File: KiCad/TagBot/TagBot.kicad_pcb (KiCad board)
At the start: 4 copper layers, 54 x 57 mm, 76 parts, among them IC101 ADXL343BCCZ-RL, J101 Conn_ST_STDC14, J102 Conn_01x06, J103 Conn_01x03, J104 Conn_01x06, J105 Conn_01x02, J106 Conn_01x08, J107 Conn_01x06, J111 Conn_01x04, SW101 SW_Push, SW102 SW_Push, U101 STM32G431CBUx, U201 ZXBM5210-SP, U301 ZXBM5210-SP, U401 MP1475S, U501 BU33SD5WG-TR, Y101 Crystal

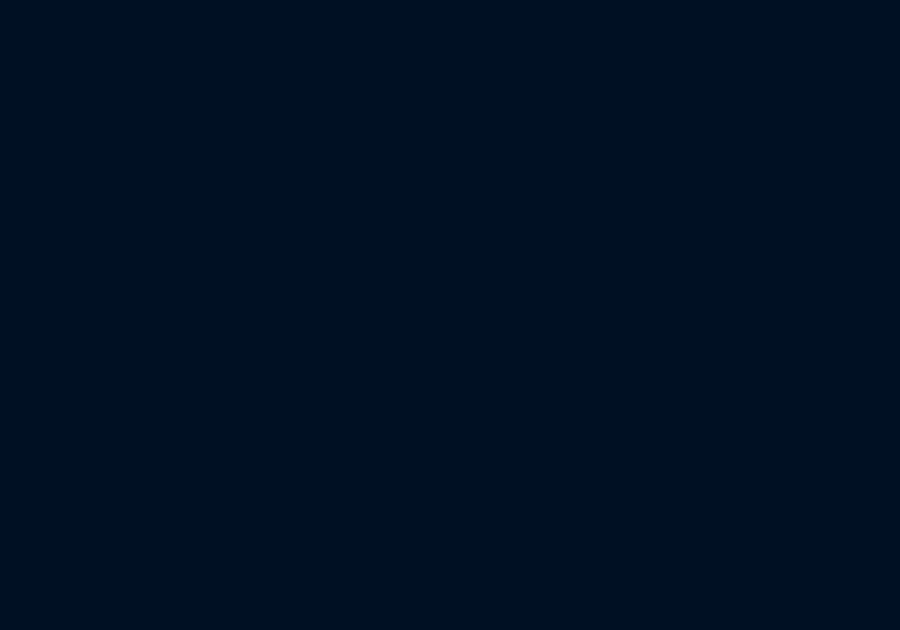
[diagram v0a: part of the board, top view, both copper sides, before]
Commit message: ajout résistance capteurs
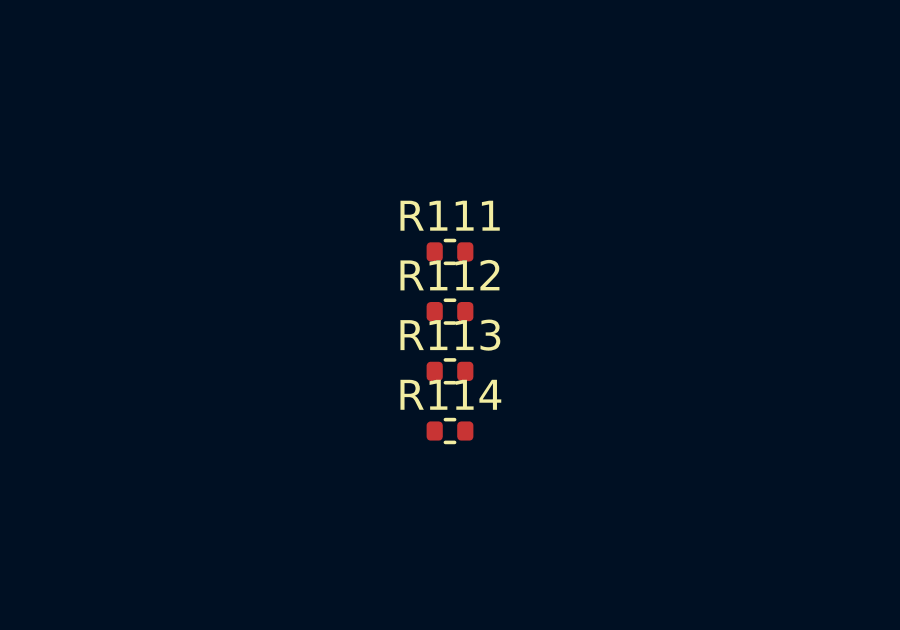
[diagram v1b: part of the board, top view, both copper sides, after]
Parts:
- added R111: 100, Resistor_SMD:R_0402_1005Metric, F.Cu at (150.0, 42.2)
- added R112: 100, Resistor_SMD:R_0402_1005Metric, F.Cu at (150.0, 44.2)
- added R113: 100, Resistor_SMD:R_0402_1005Metric, F.Cu at (150.0, 46.2)
- added R114: 100, Resistor_SMD:R_0402_1005Metric, F.Cu at (150.0, 48.1)
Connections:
- J107 pad 1: /Capteur_dist_S -> Net-(J107-Pin_1)
- J107 pad 2: /Capteur_dist_N -> Net-(J107-Pin_2)
- J107 pad 3: /Capteur_dist_W -> Net-(J107-Pin_3)
- J107 pad 4: /Capteur_dist_E -> Net-(J107-Pin_4)

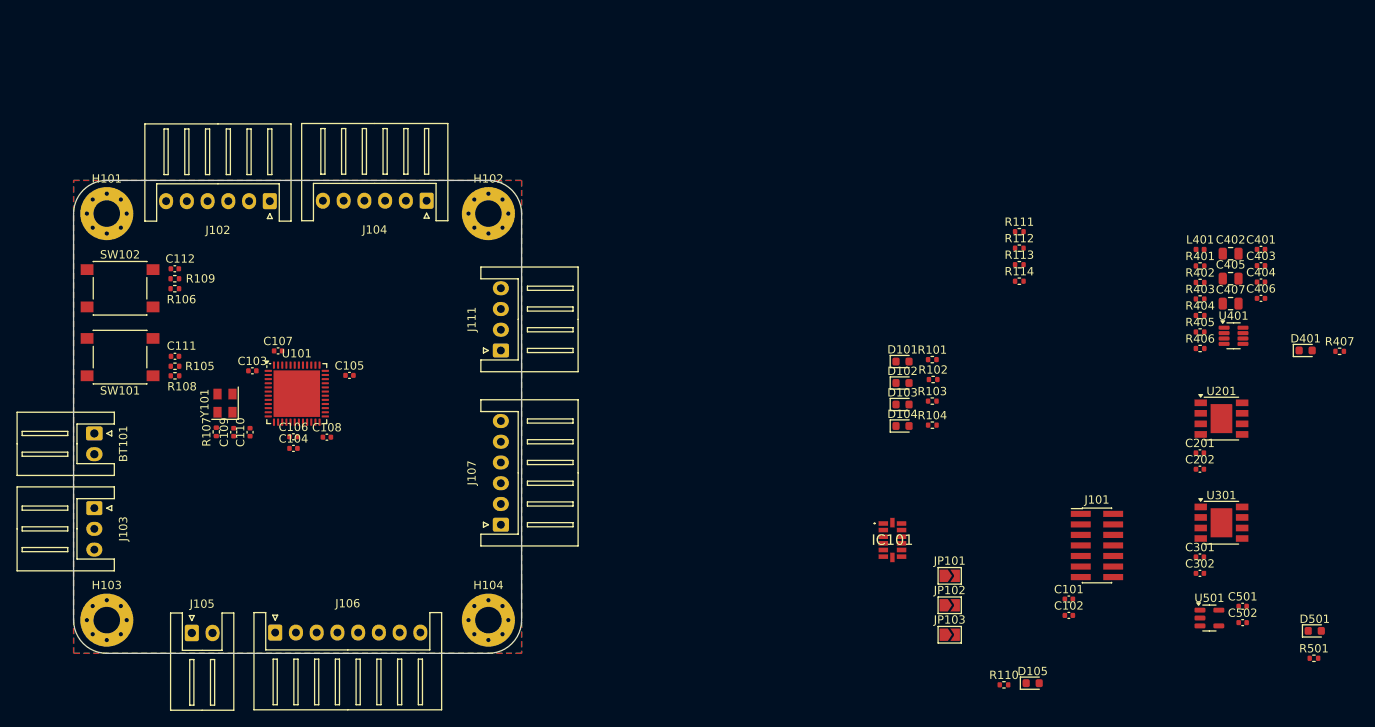
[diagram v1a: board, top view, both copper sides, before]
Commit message: correction schema kicad
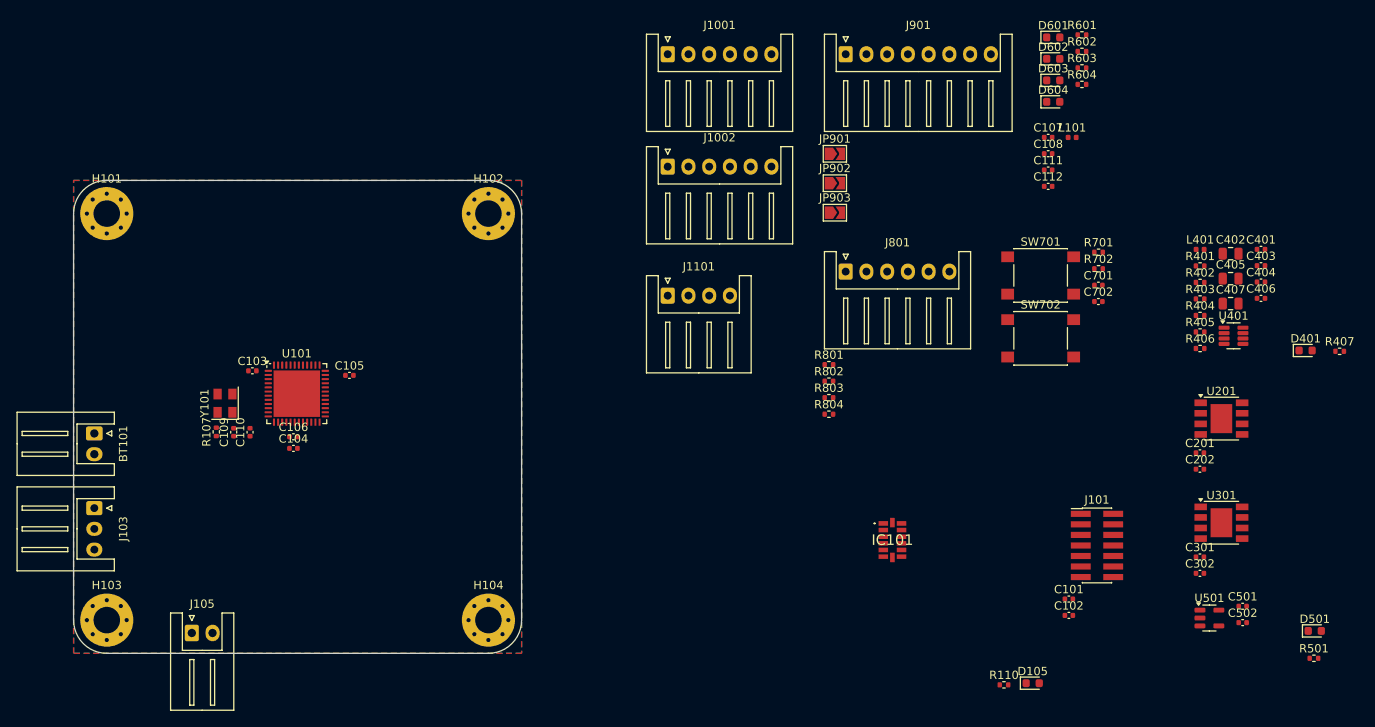
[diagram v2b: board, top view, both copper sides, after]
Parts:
- removed D101, D102, D103, D104: LED, LED_SMD:LED_0603_1608Metric
- removed J102, J104, J107: Conn_01x06, Connector_JST:JST_XH_S6B-XH-A_1x06_P2.50mm_Horizontal
- removed J106: Conn_01x08, Connector_JST:JST_XH_S8B-XH-A_1x08_P2.50mm_Horizontal
- removed J111: Conn_01x04, Connector_JST:JST_XH_S4B-XH-A_1x04_P2.50mm_Horizontal
- removed JP101, JP102, JP103: SolderJumper_2_Open, Jumper:SolderJumper-2_P1.3mm_Open_TrianglePad1.0x1.5mm
- removed R101: 1.3k, Resistor_SMD:R_0402_1005Metric
- removed R102, R103, R104, R111, R112, R113, R114: 100, Resistor_SMD:R_0402_1005Metric
- removed R105, R106: 100k, Resistor_SMD:R_0402_1005Metric
- removed R108, R109: 1k, Resistor_SMD:R_0402_1005Metric
- removed SW101, SW102: SW_Push, Button_Switch_SMD:SW_Push_1P1T_NO_6x6mm_H9.5mm
- added C701: 10n, Capacitor_SMD:C_0402_1005Metric, F.Cu at (159.5, 48.6)
- added C702: 100n, Capacitor_SMD:C_0402_1005Metric, F.Cu at (159.5, 50.6)
- added D601: LED, LED_SMD:LED_0603_1608Metric, F.Cu at (154.1, 18.8)
- added D602: LED, LED_SMD:LED_0603_1608Metric, F.Cu at (154.1, 21.4)
- added D603: LED, LED_SMD:LED_0603_1608Metric, F.Cu at (154.1, 23.9)
- added D604: LED, LED_SMD:LED_0603_1608Metric, F.Cu at (154.1, 26.5)
- added J1001: Conn_01x06, Connector_JST:JST_XH_S6B-XH-A_1x06_P2.50mm_Horizontal, F.Cu at (107.6, 20.8)
- added J1002: Conn_01x06, Connector_JST:JST_XH_S6B-XH-A_1x06_P2.50mm_Horizontal, F.Cu at (107.6, 34.3)
- added J1101: Conn_01x04, Connector_JST:JST_XH_S4B-XH-A_1x04_P2.50mm_Horizontal, F.Cu at (107.6, 49.9)
- added J801: Conn_01x06, Connector_JST:JST_XH_S6B-XH-A_1x06_P2.50mm_Horizontal, F.Cu at (129.1, 47.0)
- added J901: Conn_01x08, Connector_JST:JST_XH_S8B-XH-A_1x08_P2.50mm_Horizontal, F.Cu at (129.1, 20.8)
- added JP901: SolderJumper_2_Open, Jumper:SolderJumper-2_P1.3mm_Open_TrianglePad1.0x1.5mm, F.Cu at (127.8, 32.8)
- added JP902: SolderJumper_2_Open, Jumper:SolderJumper-2_P1.3mm_Open_TrianglePad1.0x1.5mm, F.Cu at (127.8, 36.3)
- added JP903: SolderJumper_2_Open, Jumper:SolderJumper-2_P1.3mm_Open_TrianglePad1.0x1.5mm, F.Cu at (127.8, 39.9)
- added L101: 47n, Inductor_SMD:L_0402_1005Metric, F.Cu at (156.4, 30.8)
- added R601: 300, Resistor_SMD:R_0402_1005Metric, F.Cu at (157.5, 18.5)
- added R602: 300, Resistor_SMD:R_0402_1005Metric, F.Cu at (157.5, 20.4)
- added R603: 1.3k, Resistor_SMD:R_0402_1005Metric, F.Cu at (157.5, 22.4)
- added R604: 300, Resistor_SMD:R_0402_1005Metric, F.Cu at (157.5, 24.4)
- added R701: 10k, Resistor_SMD:R_0402_1005Metric, F.Cu at (159.5, 44.7)
- added R702: 10k, Resistor_SMD:R_0402_1005Metric, F.Cu at (159.5, 46.6)
- added R801: 100, Resistor_SMD:R_0402_1005Metric, F.Cu at (127.0, 58.2)
- added R802: 100, Resistor_SMD:R_0402_1005Metric, F.Cu at (127.0, 60.2)
- added R803: 100, Resistor_SMD:R_0402_1005Metric, F.Cu at (127.0, 62.2)
- added R804: 100, Resistor_SMD:R_0402_1005Metric, F.Cu at (127.0, 64.2)
- added SW701: SW_Push, Button_Switch_SMD:SW_Push_1P1T_NO_6x6mm_H9.5mm, F.Cu at (152.6, 47.5)
- added SW702: SW_Push, Button_Switch_SMD:SW_Push_1P1T_NO_6x6mm_H9.5mm, F.Cu at (152.6, 55.0)
- C108, C111: value 100n -> 1u
- C112: value 100n -> 10n
- C201, C301: value 500n -> 1u
- C202, C302: value 500n -> 10u
- R501: value 100 -> 300
- moved C111 107.6 mm to (153.5, 34.8), turned to 0 degrees
- moved C112 105.7 mm to (153.5, 36.7), turned to 0 degrees
- moved C107 96.3 mm to (153.5, 30.8)
- moved C108 93.4 mm to (153.5, 32.8)
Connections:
- C107 pad 1: +3.3V -> GND
- C107 pad 2: GND -> +3.3VA
- C108 pad 1: +3.3V -> GND
- C108 pad 2: +3.3V -> +3.3VA
- C111 pad 1: /NRST -> GND
- C111 pad 2: GND -> +3.3VA
- C112 pad 1: /BTN_CAT_MOUSE -> GND
- C112 pad 2: GND -> +3.3VA
- C402 pad 1: /Régulateur 5V/7.2V -> /Valim
- C403 pad 1: /Régulateur 5V/7.2V -> /Valim
- J101 pad 12: /NRST -> +3.3V
- R401 pad 1: /Régulateur 5V/7.2V -> /Valim
- U101 pad 20: +3.3V -> +3.3VA
- U101 pad 21: +3.3V -> +3.3VA
- U101 pad 7: /NRST -> +3.3V
- U401 pad 2: /Régulateur 5V/7.2V -> /Valim

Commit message: placement pcb 2
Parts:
- L101: value 47n -> 39n; footprint Inductor_SMD:L_0402_1005Metric -> Inductor_SMD:L_0603_1608Metric
- L401: footprint Inductor_SMD:L_0402_1005Metric -> Library:Power Inductors - SMD WE-LQS 4.7uH
- moved R407 135.6 mm to (53.4, 66.0), turned to 180 degrees
- moved D401 134.3 mm to (50.6, 66.0)
- moved C406 131.7 mm to (48.9, 70.2), turned to -90 degrees
- moved C401 129.3 mm to (52.1, 68.3)
- moved C405 128.1 mm to (50.0, 73.5), turned to -90 degrees
- moved C407 125.0 mm to (52.5, 73.5), turned to -90 degrees
- moved C402 123.7 mm to (56.0, 76.9)
- moved L401 123.4 mm to (53.1, 78.3), turned to 180 degrees
- moved C404 123.4 mm to (58.5, 74.2), turned to -90 degrees
- moved C403 123.4 mm to (58.5, 72.2), turned to 90 degrees
- moved R405 123.0 mm to (49.6, 68.3)
- moved R406 122.3 mm to (50.2, 70.1), turned to -90 degrees
- moved R404 121.4 mm to (51.8, 70.1), turned to 90 degrees
- moved U401 121.2 mm to (56.0, 73.1), turned to 90 degrees
- moved R402 120.8 mm to (53.0, 70.1), turned to -90 degrees
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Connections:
- C101 pad 1: +3.3V -> GND
- C102 pad 1: +3.3V -> GND
- C702 pad 1: +3.3V -> /NRST
- J101 pad 12: +3.3V -> /NRST
- SW702 pad 1: +3.3V -> /NRST
- U101 pad 7: +3.3V -> /NRST

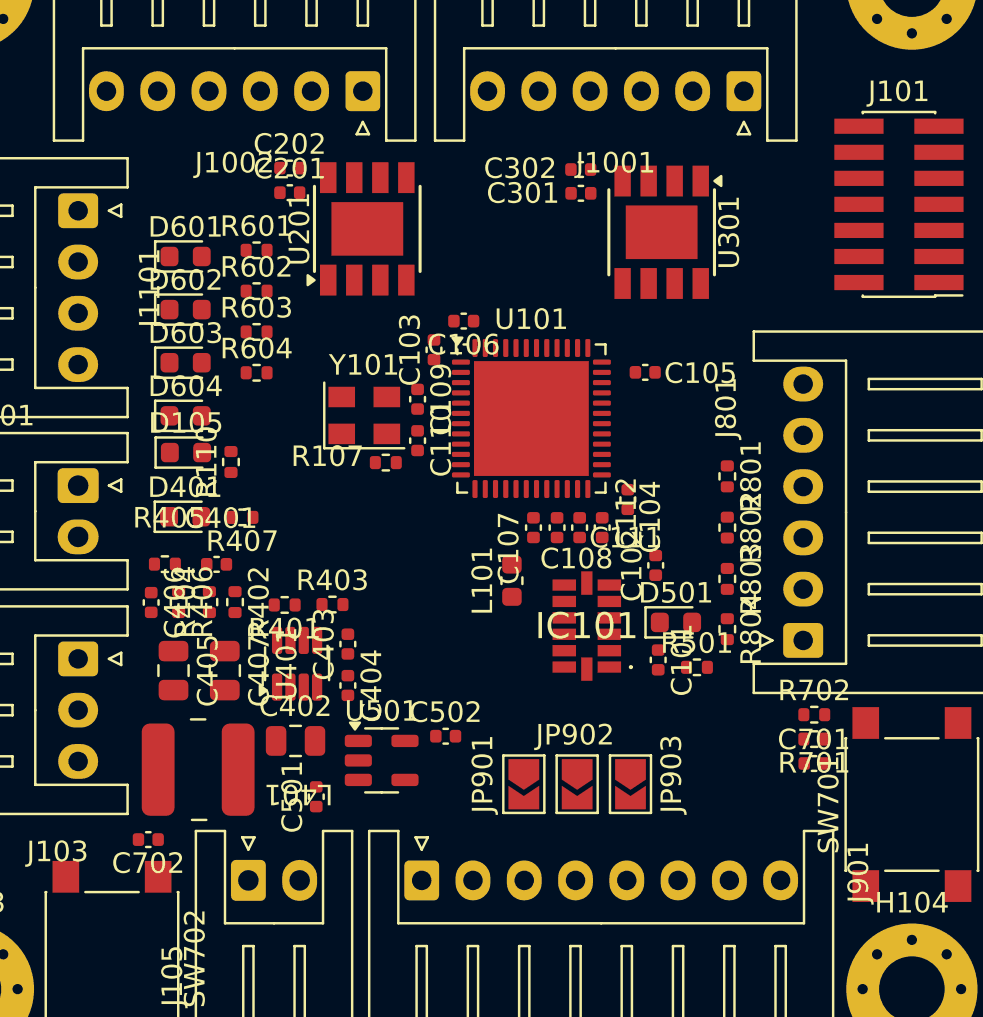
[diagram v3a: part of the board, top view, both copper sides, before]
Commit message: updated pcb placement
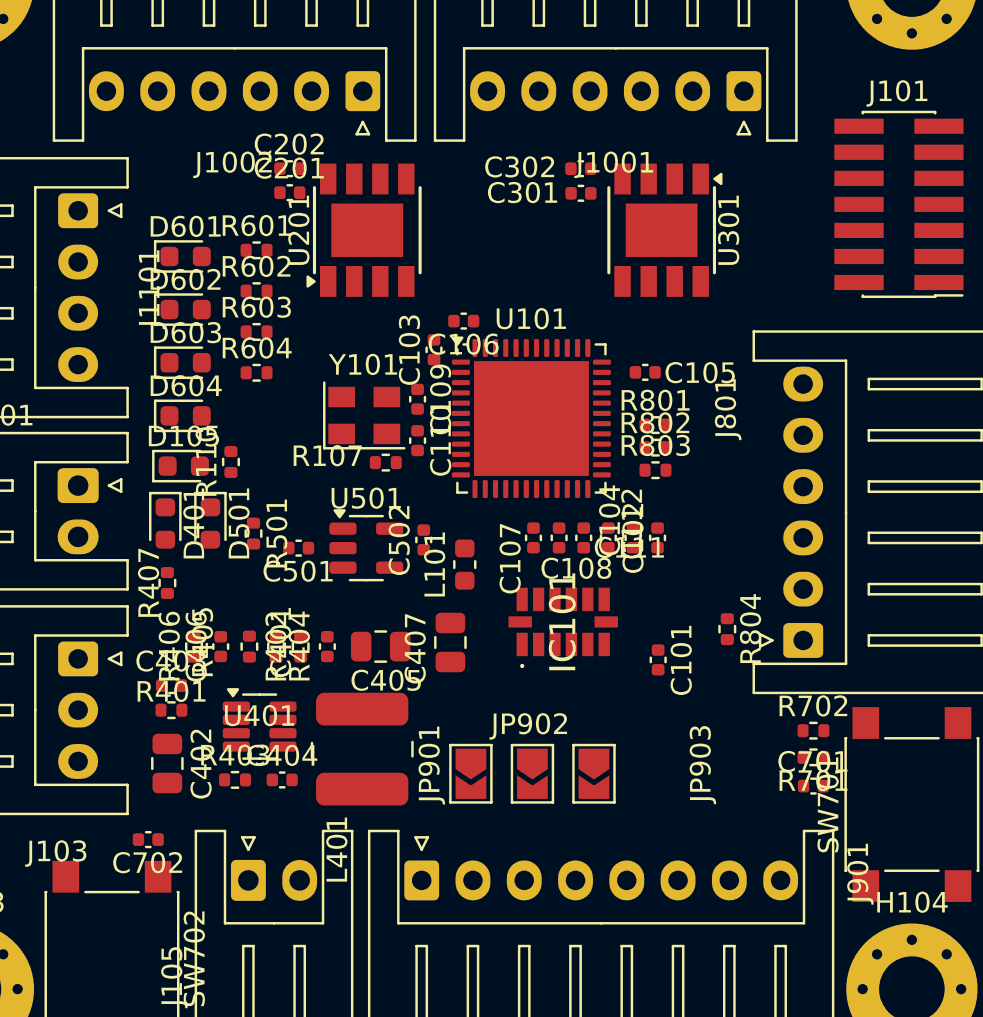
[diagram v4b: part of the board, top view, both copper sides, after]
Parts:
- moved D501 23.2 mm to (51.8, 66.3), turned to -90 degrees
- moved R501 22.6 mm to (53.9, 66.8), turned to -90 degrees
- moved C501 12.2 mm to (56.1, 67.5), turned to 180 degrees
- moved C407 11.1 mm to (63.5, 72.1), turned to 90 degrees
- moved U501 10.4 mm to (59.4, 67.5)
- moved C405 10.2 mm to (60.1, 72.3), turned to 180 degrees
- moved R403 9.78 mm to (53.0, 78.8)
- moved C502 9.63 mm to (62.2, 67.1), turned to 90 degrees
- moved C403 8.83 mm to (49.9, 74.2), turned to 0 degrees
- moved R401 7.54 mm to (49.9, 75.4), turned to 0 degrees
- moved C401 6.73 mm to (57.5, 72.3), turned to 90 degrees
- moved R803 6.35 mm to (73.5, 63.7), turned to 0 degrees
- moved C402 6.35 mm to (49.7, 78.0), turned to -90 degrees
- moved L401 6.12 mm to (59.2, 79.2), turned to 90 degrees
- moved R405 5.76 mm to (53.7, 72.3), turned to 90 degrees
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
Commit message: routing
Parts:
- moved C102 10.2 mm to (68.6, 75.9), turned to 180 degrees
- moved R601 8.32 mm to (54.1, 61.3)
- moved D601 8.03 mm to (50.9, 61.3)
- moved D604 4.80 mm to (50.9, 56.3)
- moved R602 4.36 mm to (54.0, 59.3)
- moved R407 4.34 mm to (54.0, 68.5), turned to 180 degrees
- moved D603 4.29 mm to (50.9, 54.2)
- moved C101 3.59 mm to (71.6, 75.9), turned to 0 degrees
- moved D602 3.48 mm to (51.0, 59.3)
- moved R603 2.78 mm to (54.0, 54.2)
- moved R604 2.69 mm to (54.0, 56.3)
- moved D401 2.56 mm to (51.0, 68.5), turned to 0 degrees
- moved R110 2.08 mm to (51.2, 64.7), turned to 0 degrees
- moved L101 2.02 mm to (66.1, 67.6)
- moved R403 2.02 mm to (55.0, 78.3), turned to 180 degrees
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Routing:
- net GND: track 0.00 -> 33.3 mm, vias 0 -> 51
- net +5V: track 0.00 -> 14.3 mm
- net +3.3V: track 0.00 -> 14.0 mm, vias 0 -> 7
- net Net-(R701-Pad1): track 0.00 -> 11.2 mm
- net /Valim: track 0.00 -> 10.7 mm
- net Net-(J801-Pin_2): track 0.00 -> 8.86 mm
- net +3.3VA: track 0.00 -> 8.58 mm
- net Net-(J801-Pin_3): track 0.00 -> 8.28 mm
- net Net-(J801-Pin_4): track 0.00 -> 7.70 mm
- net Net-(U401-VCC): track 0.00 -> 5.56 mm
- net /Vbatterie: track 0.00 -> 5.27 mm
- net Net-(U401-SW): track 0.00 -> 4.75 mm
- net Net-(C406-Pad1): track 0.00 -> 3.99 mm
- net Net-(U401-FB): track 0.00 -> 3.74 mm
- net Net-(J801-Pin_1): track 0.00 -> 3.60 mm
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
